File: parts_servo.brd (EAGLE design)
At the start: 50 x 27.1 mm, 43 parts, among them Q110 PMDPB28UN, Q120 PMDPB28UN, U1 MCP1703-3302, U100 RT9625A, U20 sn65hvd72, U50 nRF51822, X60 CX3225GB16000P0HPQCC

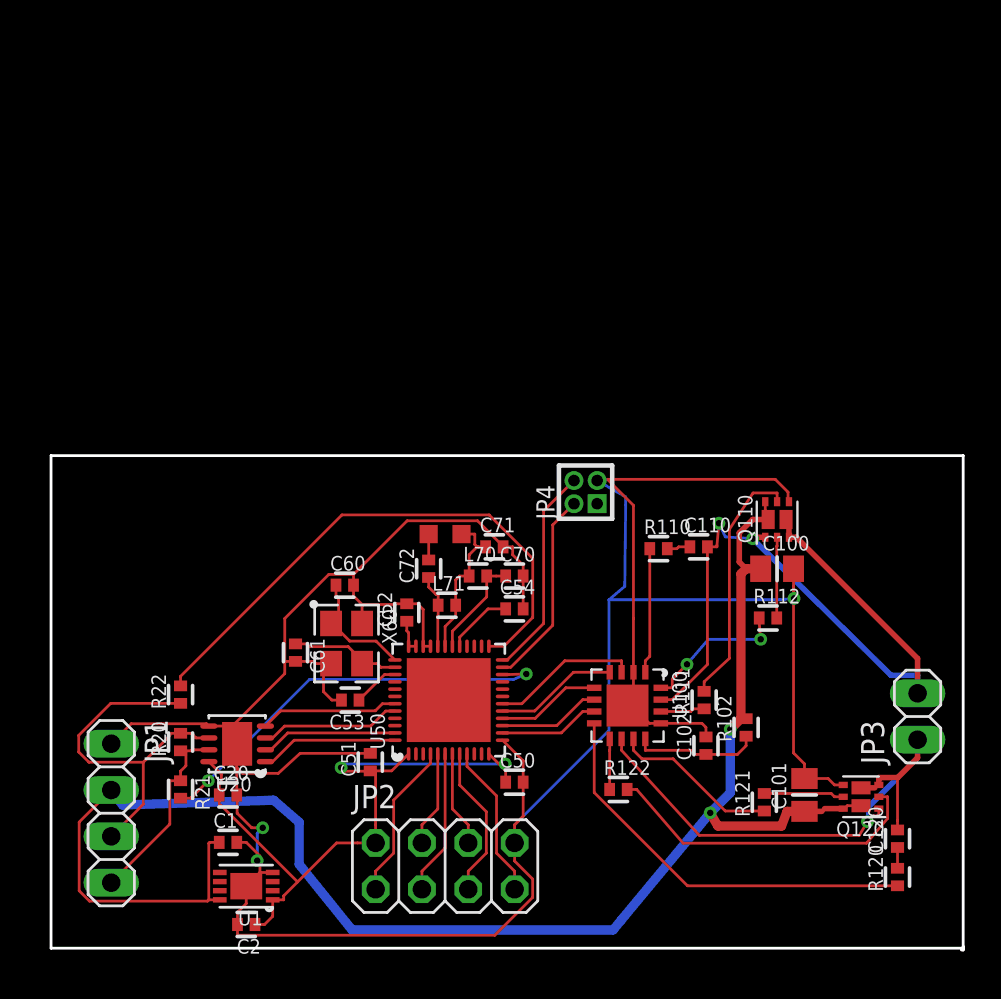
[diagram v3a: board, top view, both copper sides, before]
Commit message: Connect NRF center pad to GND.  Add ground pour on bottom of board to improve current return from motor FETs.
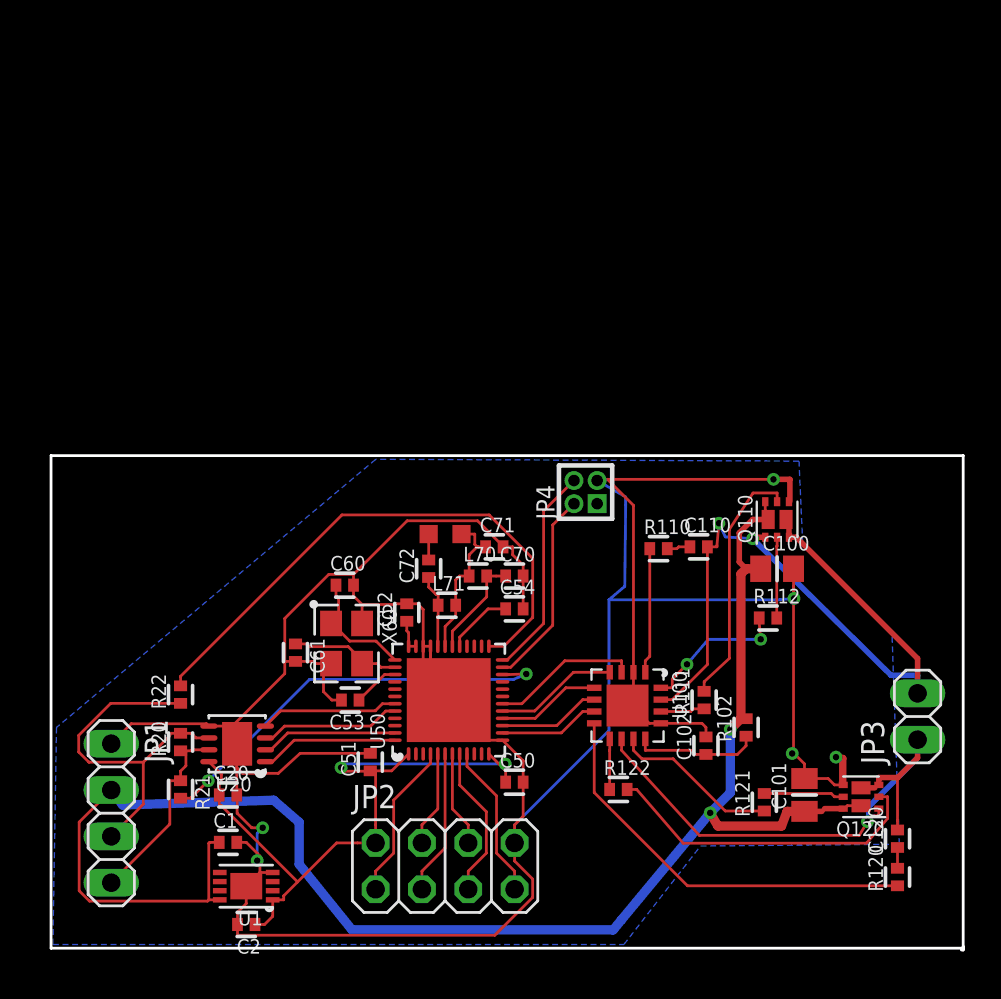
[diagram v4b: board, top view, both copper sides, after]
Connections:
- net GND: now also U50.PAD
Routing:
- net GND: track 175.8 -> 180.4 mm, vias 3 -> 6
- added copper zone on layer 16, net GND
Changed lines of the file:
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@@
 <wire x1="11.4" y1="6.4" x2="11.7" y2="6.7" width="0.1524" layer="16"/>
 <wire x1="11.4" y1="4.9" x2="11.4" y2="6.4" width="0.1524" layer="16"/>
-<wire x1="11.5" y1="4.9" x2="11.4" y2="4.9" width="0.1524" layer="1"/>
+<wire x1="11.55" y1="4.9" x2="11.4" y2="4.9" width="0.1524" layer="1"/>
 <wire x1="10.3" y1="8.5" x2="10.28" y2="8.5" width="0.1524" layer="1"/>
-<wire x1="11.5" y1="4.9" x2="11.55" y2="4.9" width="0.1524" layer="1"/>
 <via x="11.7" y="6.7" extent="1-16" drill="0.35" diameter="0.6358"/>
 <via x="11.4" y="4.9" extent="1-16" drill="0.35" diameter="0.6358"/>
-<wire x1="32.025" y1="15.225" x2="32.025" y2="18.1756" width="0.1524" layer="1"/>
 <wire x1="40.55" y1="24.575" x2="40.525" y2="24.575" width="0.1524" layer="1"/>
-<wire x1="40.525" y1="24.575" x2="40.5" y2="24.6" width="0.1524" layer="1"/>
-<wire x1="40.5" y1="24.6" x2="40.5" y2="25.1" width="0.1524" layer="1"/>
-<wire x1="40.5" y1="25.1" x2="39.8" y2="25.8" width="0.1524" layer="1"/>
-<wire x1="39.8" y1="25.8" x2="30.6" y2="25.8" width="0.1524" layer="1"/>
+<wire x1="40.525" y1="24.575" x2="40.6" y2="24.6" width="0.1524" layer="1"/>
+<wire x1="40.6" y1="24.6" x2="40.6" y2="25.8" width="0.3048" layer="1"/>
+<wire x1="40.6" y1="25.8" x2="39.7" y2="25.8" width="0.3048" layer="1"/>
+<wire x1="39.7" y1="25.8" x2="30.6" y2="25.8" width="0.1524" layer="1"/>
 <wire x1="30.6" y1="25.8" x2="30.1" y2="25.8" width="0.1524" layer="1"/>
 <wire x1="30.1" y1="25.8" x2="30.035" y2="25.735" width="0.1524" layer="1"/>
-<wire x1="32.025" y1="18.1756" x2="32.025" y2="24.375" width="0.1524" layer="1"/>
+<wire x1="32.025" y1="15.225" x2="32.025" y2="24.375" width="0.1524" layer="1"/>
 <wire x1="32.025" y1="24.375" x2="30.6" y2="25.8" width="0.1524" layer="1"/>
+<polygon width="0.4064" layer="16" isolate="0.4064">
+<vertex x="0.2" y="0.3"/>
+<vertex x="31.5" y="0.3"/>
+<vertex x="35.7" y="5.7"/>
+<vertex x="46.6" y="5.8"/>
+<vertex x="46.2" y="17.3"/>
+<vertex x="41.3" y="22.3"/>
+<vertex x="41.1" y="26.8"/>
+<vertex x="17.9" y="26.9"/>
+<vertex x="0.4" y="12.2"/>
+</polygon>
+<via x="39.7" y="25.8" extent="1-16" drill="0.35"/>
+<via x="40.727" y="10.7733" extent="1-16" drill="0.35" diameter="0.6858"/>
+<via x="43.127" y="10.5733" extent="1-16" drill="0.35" diameter="0.6858"/>
+<contactref element="U50" pad="PAD"/>
+<wire x1="20.9" y1="16.4" x2="20.9" y2="15.8" width="0.154" layer="1"/>
+<wire x1="20.9" y1="16.4" x2="20.9" y2="15.8" width="0.154" layer="1"/>
+<wire x1="20.5" y1="16.4" x2="20.5" y2="15.8" width="0.154" layer="1"/>
+<wire x1="24.1" y1="11.5" x2="24.7" y2="11.5" width="0.154" layer="1"/>
+<wire x1="43.2" y1="10.5" x2="43.5" y2="10.5" width="0.4064" layer="1"/>
+<wire x1="43.5" y1="10.5" x2="43.5" y2="9.1" width="0.4064" layer="1"/>
+<wire x1="43.525" y1="9.05" x2="43.5" y2="9.1" width="0" layer="19" extent="1-1"/>
+<wire x1="24.7" y1="11.5" x2="24.7741" y2="11.5" width="0" layer="19" extent="1-1"/>
+<wire x1="20.9" y1="16.4" x2="20.9" y2="16.55" width="0" layer="19" extent="1-1"/>
+<wire x1="20.5" y1="16.4" x2="20.5" y2="16.65" width="0" layer="19" extent="1-1"/>
+<wire x1="21.9" y1="13.7" x2="20.9" y2="15.8" width="0" layer="19" extent="1-1"/>
 </signal>
 <signal name="HSCLK_IN">

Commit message: Clean up silkscreen text
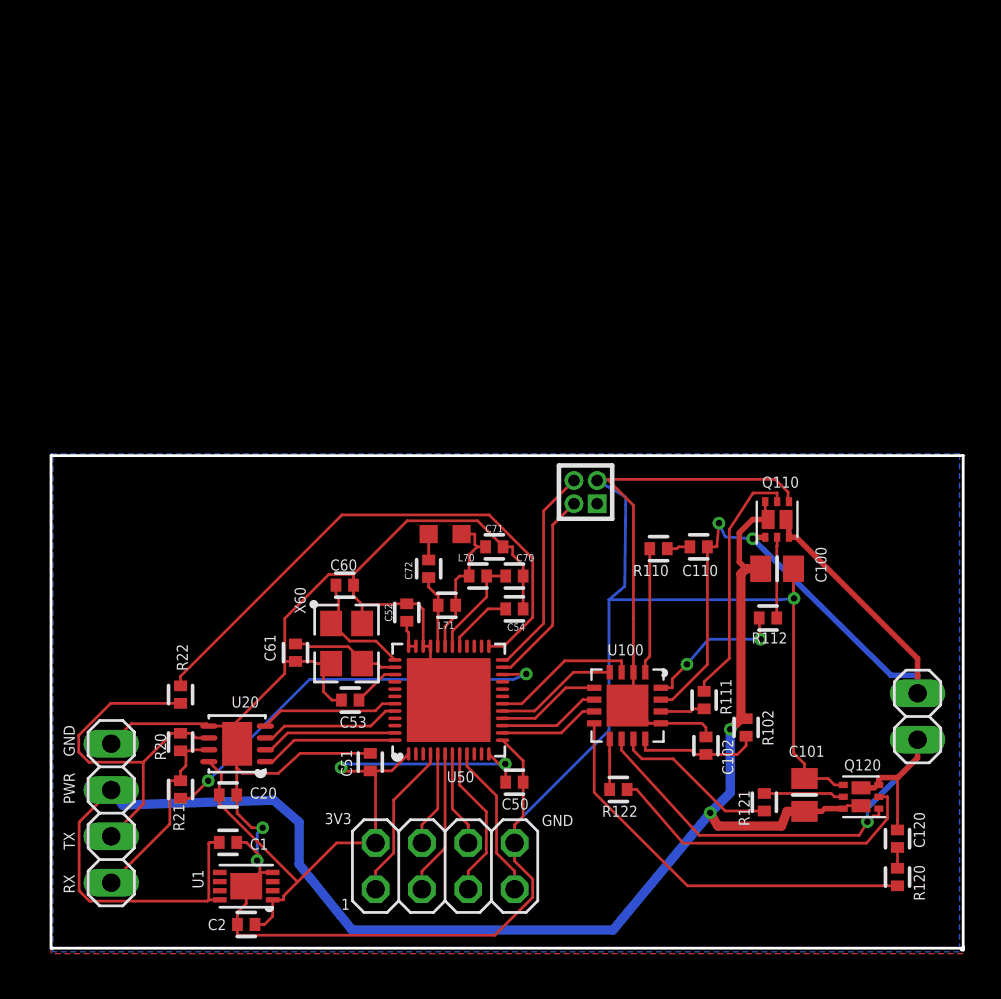
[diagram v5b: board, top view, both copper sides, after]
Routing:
- net GND: track 180.4 -> 179.6 mm, vias 6 -> 3
- added copper zone on layer 1, net GND
- added copper zone on layer 16, net N$1
- removed copper zone on layer 16, net GND
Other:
- board text added: "1"
- board text added: "3V3"
- board text added: "GND"
- board text added: "PWR"
- board text added: "RX"
- board text added: "TX"

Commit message: Set bottom fill to net GND.  Added mounting holes and a few extra GND vias.
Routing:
- net GND: vias 3 -> 7
- added copper zone on layer 16, net GND
- removed copper zone on layer 16, net N$1
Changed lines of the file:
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@@
 <text x="15.1" y="6.9" size="0.6096" layer="25" font="vector" ratio="15">3V3</text>
 <text x="27" y="6.8" size="0.6096" layer="25" font="vector" ratio="15">GND</text>
+<hole x="3.1" y="24.1" drill="3.2"/>
+<hole x="47.1" y="24.1" drill="3.2"/>
 </plain>
 <attributes>
@@
 <wire x1="20.9" y1="15.1" x2="21.9" y2="15.1" width="0.4064" layer="1"/>
 <wire x1="21.9" y1="15.1" x2="21.9" y2="13.7" width="0.4064" layer="1"/>
+<via x="10.6" y="15.4" extent="1-16" drill="0.5"/>
+<via x="28.5" y="17.1" extent="1-16" drill="0.5"/>
+<via x="42" y="23.7" extent="1-16" drill="0.5" shape="square"/>
+<via x="44.4" y="10.5" extent="1-16" drill="0.5"/>
+<polygon width="0.4064" layer="16">
+<vertex x="0.1" y="27.2"/>
+<vertex x="49.9" y="27.2"/>
+<vertex x="49.9" y="-0.1"/>
+<vertex x="0.2" y="-0.1"/>
+<vertex x="0.2" y="27.1"/>
+</polygon>
 </signal>
 <signal name="HSCLK_IN">
@@
 <wire x1="24.5193" y1="5.3114" x2="25.51" y2="4.3207" width="0.1524" layer="1"/>
 </signal>
-<signal name="N$1">
-<polygon width="0.4064" layer="16">
-<vertex x="0.1" y="27.2"/>
-<vertex x="49.9" y="27.2"/>
-<vertex x="49.9" y="-0.1"/>
-<vertex x="0.2" y="-0.1"/>
-<vertex x="0.2" y="27.1"/>
-</polygon>
-</signal>
 </signals>

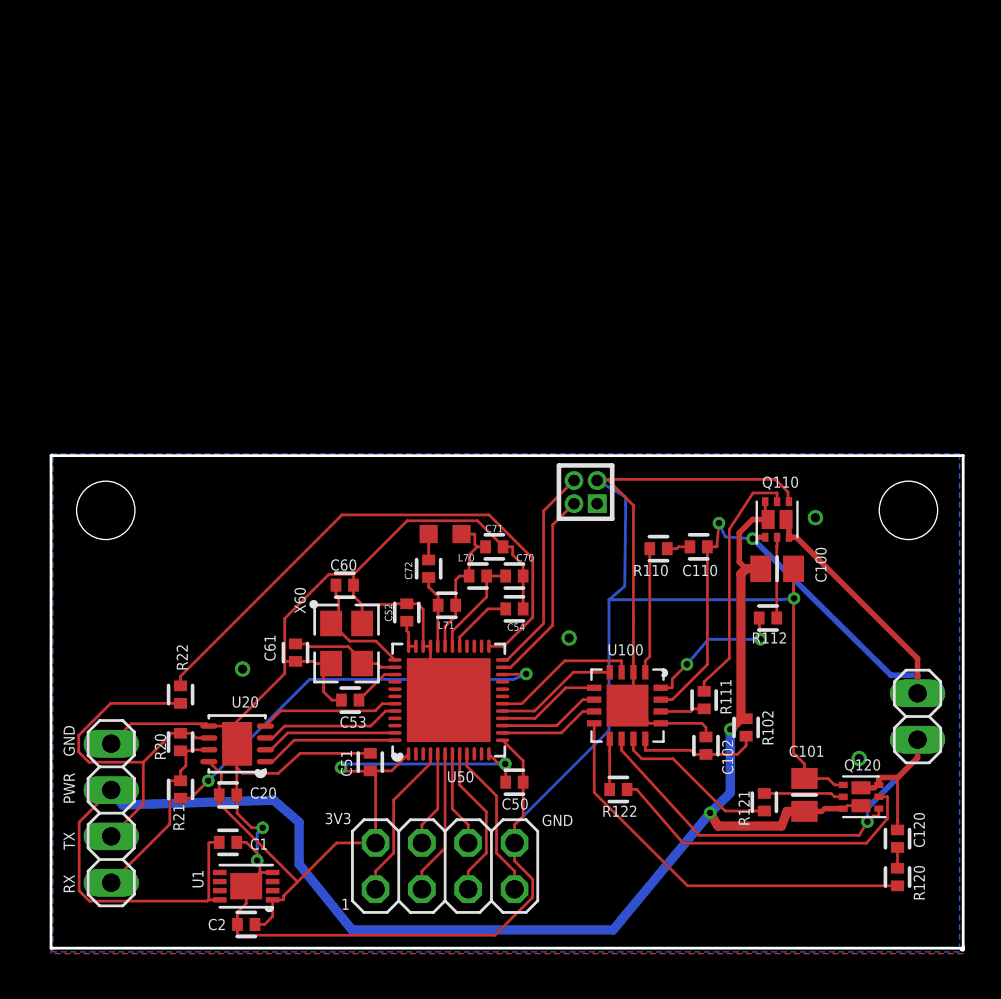
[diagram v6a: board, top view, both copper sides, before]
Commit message: Second rev of board design.  Shrink to servo case size
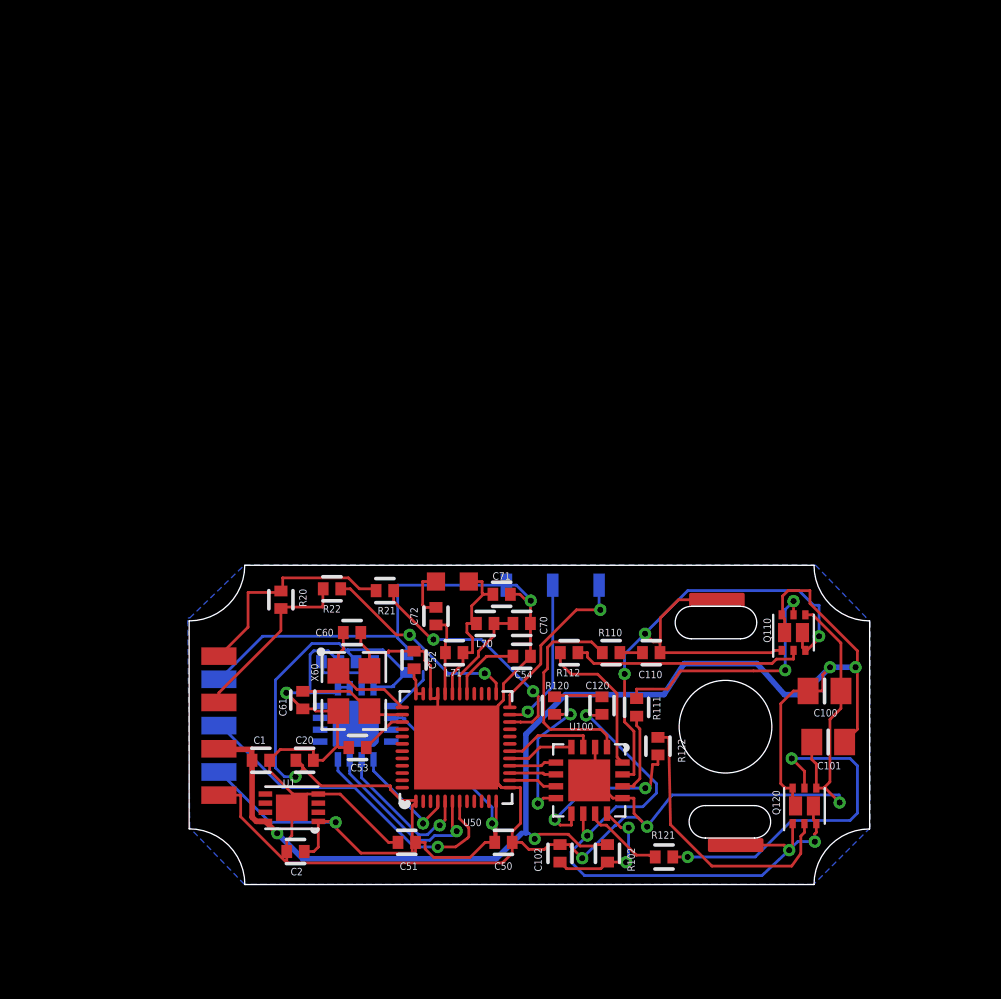
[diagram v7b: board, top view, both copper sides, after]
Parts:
- removed U20: sn65hvd72, parts_servo:DFN-8(3X3)+EP
- added C203: .1uF, rcl_custom:0402-B
- added C204: 4u7, rcl_custom:0402-B
- added JP5: POT, parts_servo:SMD_1X3_PADS
- added R201: 15, rcl_custom:0402-B
- added U200: AS5050, parts_servo:QFN16_4X4
- JP1: value I/O -> M01; device pinhead:1X04 -> parts_servo:SMDMOTOR
- JP2: value Sensor -> Input; device pinhead:2X04 -> parts_servo:SMD_1X4_HEADER
- JP3: value Motor -> M01; device pinhead:1X02 -> parts_servo:SMDMOTOR
- JP4: device parts_servo:PINHEADER-2X2-0.05_IN -> parts_servo:SMD_1X3_HEADER
- moved JP1 34.3 mm to (37.6, 5.75), turned to 0 degrees
- moved R120 21.0 mm to (27.7, 13.4)
- moved C120 17.8 mm to (30.3, 13.4), turned to 270 degrees
- moved R21 15.6 mm to (18.4, 19.7), turned to 0 degrees
- moved JP2 14.6 mm to (9.30, 12.3), turned to 180 degrees
- moved JP3 12.7 mm to (36.6, 19.2), turned to 0 degrees
- moved R112 11.1 mm to (28.5, 16.3)
- moved R102 10.3 mm to (30.6, 5.30)
- moved R22 10.1 mm to (15.5, 19.8), turned to 0 degrees
- moved C102 9.94 mm to (28.0, 5.30)
- moved R20 9.54 mm to (12.7, 19.2), turned to 270 degrees
- moved C100 7.19 mm to (42.5, 14.2)
- moved C110 6.36 mm to (33.0, 16.3)
- moved Q110 6.26 mm to (40.8, 17.4)
- moved R121 6.26 mm to (33.7, 5.10), turned to 0 degrees
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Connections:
- removed net DIFFERENTIAL_INPUT: U20.1, U50.48
- removed net DIFFERENTIAL_INPUT_EN: U20.2, U50.47
- removed net DIFFERENTIAL_OUTPUT: U20.4, U50.43
- removed net DIFFERENTIAL_OUTPUT_EN: U20.3, U50.44
- removed net SENSOR1: JP2.1, U50.4
- removed net SENSOR2: JP2.3, U50.6
- removed net SENSOR3: JP2.4, U50.5
- removed net SENSOR4: JP2.5, U50.8
- removed net SENSOR5: JP2.6, U50.7
- removed net SENSOR6: JP2.7, U50.9
- new net N$1: U200.1, U50.4
- new net N$3: U200.2, U50.5
- new net N$4: U200.3, U50.6
- new net N$5: JP5.2, U200.4, U50.7
- new net N$6: C204.2, R201.1, U200.11
- net 3.3V: now also C203.1, JP5.3, R201.2, U200.12, U200.14; no longer JP2.2, U20.8
- net D1/TX: now also JP2.3; no longer JP1.3, U20.6
- net D2/RX: now also JP2.4; no longer JP1.4, U20.7
- net GND: now also C203.2, C204.1, JP2.1, JP4.P$3, JP5.1, U200.10, U200.13, U200.9; no longer JP1.1, JP2.8, JP4.3, U20.5, U20.PAD
- net MOTOR1: now also JP1.1; no longer JP3.1
- net MOTOR2: now also JP3.1; no longer JP3.2
- net POWER_IN: now also JP2.2; no longer JP1.2
- net SWDCLK: now also JP4.P$2; no longer JP4.4
- net SWDIO: now also JP4.P$1; no longer JP4.2
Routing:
- net GND: track 179.6 -> 150.6 mm, vias 7 -> 5
- net 3.3V: track 37.6 -> 63.4 mm, vias 2 -> 3
- net N$5: track 0.00 -> 20.7 mm, vias 0 -> 1
- net UNIPOLAR_OUTPUT: track 30.8 -> 11.2 mm, vias 0 -> 2
- net QLGATE1: track 4.40 -> 19.4 mm, vias 0 -> 2
- net BOOT1: track 22.5 -> 7.79 mm, vias 0 -> 2
- net POWER_IN: track 88.3 -> 77.5 mm, vias 2 -> 4
- net D1/TX: track 20.2 -> 9.91 mm
- net N$4: track 0.00 -> 10.1 mm, vias 0 -> 1
- net UNIPOLAR_INPUT: track 23.0 -> 13.4 mm
- net SENSOR1: track 8.67 -> 0.00 mm
- net SENSOR6: track 8.50 -> 0.00 mm
- net SENSOR4: track 8.44 -> 0.00 mm
- net QUGATE2: track 4.43 -> 12.8 mm
- net N$3: track 0.00 -> 8.23 mm, vias 0 -> 1
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- removed copper zone on layer 1, net GND
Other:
- board size 50 x 27.1 mm -> 37.3 x 17.5 mm
- board text removed: "1"
- board text removed: "3V3"
- board text removed: "GND"
- board text removed: "PWR"
- board text removed: "RX"
- board text removed: "TX"
